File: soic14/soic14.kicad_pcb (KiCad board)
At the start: 2 copper layers, 15.2 x 17.8 mm, 2 parts, among them J1 bb2x7, U1 u2x7

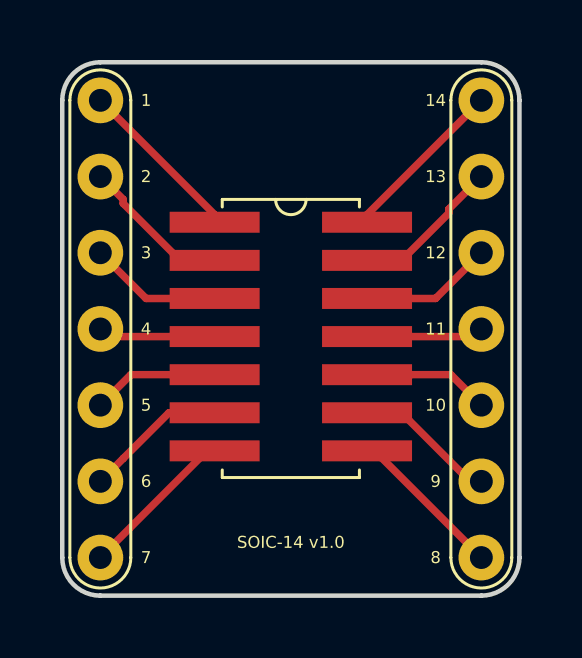
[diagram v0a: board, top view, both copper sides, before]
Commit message: Updated SOIC_SOP-SO footprints, added MSOP-TSSOP footprints
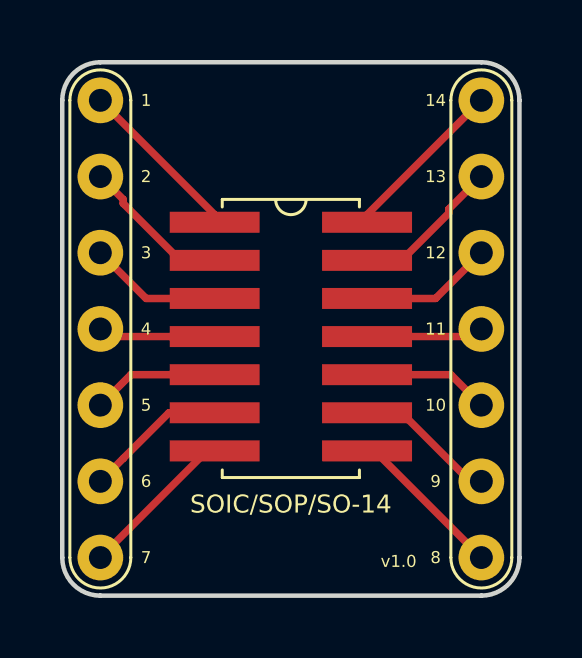
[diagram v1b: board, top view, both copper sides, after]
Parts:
- U1: value u2x7 -> SOIC/SOP/SO-14; footprint DevPc:soic-14 -> DevPcb:soic_sop_so-14
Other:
- board text added: "v1.0"
- board text removed: "SOIC-14 v1.0"
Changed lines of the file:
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@@
     (pad_to_mask_clearance 0.2)
     (aux_axis_origin 0 0)
-    (visible_elements FFFFFF7F)
+    (visible_elements 7FFFFFFF)
     (pcbplotparams
       (layerselection 0x010fc_ffffffff)
@@
     (add_net "Net-(J1-Pad9)")
   )
+  (module DevPcb:soic_sop_so-14 (layer F.Cu)
+    (at 138.176 94.107)
+    (tags "soic soic14 soic-14 soic-14-n sop so jedec")
+    (attr smd)
+    (fp_text reference U1 (at 0 11.684) (layer F.SilkS) hide
+      (effects (font (size 0.4 0.4) (thickness 0.1)))
+    )
+    (fp_text value SOIC/SOP/SO-14 (at 0 10.668) (layer F.SilkS)
+      (effects (font (size 0.6 0.6) (thickness 0.15)))
+    )
+    (fp_arc (start 0 0.508) (end -0.508 0.508) (angle -180) (layer F.SilkS) (width 0.1))
+    (fp_line (start 2.286 9.525) (end 2.286 9.779) (layer F.SilkS) (width 0.1))
+    (fp_line (start 2.286 9.779) (end -2.286 9.779) (layer F.SilkS) (width 0.1))
+    (fp_line (start -2.286 9.525) (end -2.286 9.779) (layer F.SilkS) (width 0.1))
+    (fp_line (start 2.286 0.508) (end 2.286 0.762) (layer F.SilkS) (width 0.1))
+    (fp_line (start -2.286 0.508) (end -2.286 0.762) (layer F.SilkS) (width 0.1))
+    (fp_line (start -2.286 0.508) (end 2.286 0.508) (layer F.SilkS) (width 0.1))
+    (pad 9 smd rect (at 2.54 7.62 90) (size 0.7 3) (layers F.Cu F.Paste F.Mask)
+      (net 9 "Net-(J1-Pad9)") (solder_mask_margin 0.1))
+    (pad 10 smd rect (at 2.54 6.35 90) (size 0.7 3) (layers F.Cu F.Paste F.Mask)
+      (net 10 "Net-(J1-Pad10)") (solder_mask_margin 0.1))
+    (pad 12 smd rect (at 2.54 3.81 90) (size 0.7 3) (layers F.Cu F.Paste F.Mask)
+      (net 12 "Net-(J1-Pad12)") (solder_mask_margin 0.1))
+    (pad 11 smd rect (at 2.54 5.08 90) (size 0.7 3) (layers F.Cu F.Paste F.Mask)
+      (net 11 "Net-(J1-Pad11)") (solder_mask_margin 0.1))
+    (pad 8 smd rect (at 2.54 8.89 90) (size 0.7 3) (layers F.Cu F.Paste F.Mask)
+      (net 8 "Net-(J1-Pad8)") (solder_mask_margin 0.1))
+    (pad 7 smd rect (at -2.54 8.89 90) (size 0.7 3) (layers F.Cu F.Paste F.Mask)
+      (net 7 "Net-(J1-Pad7)") (solder_mask_margin 0.1))
+    (pad 6 smd rect (at -2.54 7.62 90) (size 0.7 3) (layers F.Cu F.Paste F.Mask)
+      (net 6 "Net-(J1-Pad6)") (solder_mask_margin 0.1))
+    (pad 5 smd rect (at -2.54 6.35 90) (size 0.7 3) (layers F.Cu F.Paste F.Mask)
+      (net 5 "Net-(J1-Pad5)") (solder_mask_margin 0.1))
+    (pad 13 smd rect (at 2.54 2.54 90) (size 0.7 3) (layers F.Cu F.Paste F.Mask)
+      (net 13 "Net-(J1-Pad13)") (solder_mask_margin 0.1))
+    (pad 14 smd rect (at 2.54 1.27 90) (size 0.7 3) (layers F.Cu F.Paste F.Mask)
+      (net 14 "Net-(J1-Pad14)") (solder_mask_margin 0.1))
+    (pad 4 smd rect (at -2.54 5.08 90) (size 0.7 3) (layers F.Cu F.Paste F.Mask)
+      (net 4 "Net-(J1-Pad4)") (solder_mask_margin 0.1))
+    (pad 3 smd rect (at -2.54 3.81 90) (size 0.7 3) (layers F.Cu F.Paste F.Mask)
+      (net 3 "Net-(J1-Pad3)") (solder_mask_margin 0.1))
+    (pad 2 smd rect (at -2.54 2.54 90) (size 0.7 3) (layers F.Cu F.Paste F.Mask)
+      (net 2 "Net-(J1-Pad2)") (solder_mask_margin 0.1))
+    (pad 1 smd rect (at -2.54 1.27 90) (size 0.7 3) (layers F.Cu F.Paste F.Mask)
+      (net 1 "Net-(J1-Pad1)") (solder_mask_margin 0.1))
+    (model ${KISYS3DMOD}/Package_SO.3dshapes/SOIC-14_3.9x8.7mm_P1.27mm.step
+      (offset (xyz 0 -5.1 0))
+      (scale (xyz 1 1 1))
+      (rotate (xyz 0 0 0))
+    )
+  )
   (module DevPc:bb_2x7 (layer F.Cu)
     (at 131.826 91.313)
@@
       (net 14 "Net-(J1-Pad14)"))
   )
-  (module DevPc:soic-14 (layer F.Cu)
-    (at 138.176 94.107)
-    (tags "soic soic14 soic-14 soic-14-n jedec")
-    (attr smd)
-    (fp_text reference U1 (at 0.254 10.287) (layer F.SilkS) hide
-      (effects (font (size 0.4 0.4) (thickness 0.1)))
-    )
-    (fp_text value u2x7 (at 0 -0.5) (layer F.Fab) hide
-      (effects (font (size 1 1) (thickness 0.15)))
-    )
-    (fp_line (start -2.286 0.508) (end 2.286 0.508) (layer F.SilkS) (width 0.1))
-    (fp_line (start -2.286 0.508) (end -2.286 0.762) (layer F.SilkS) (width 0.1))
-    (fp_line (start 2.286 0.508) (end 2.286 0.762) (layer F.SilkS) (width 0.1))
-    (fp_line (start -2.286 9.525) (end -2.286 9.779) (layer F.SilkS) (width 0.1))
-    (fp_line (start 2.286 9.779) (end -2.286 9.779) (layer F.SilkS) (width 0.1))
-    (fp_line (start 2.286 9.525) (end 2.286 9.779) (layer F.SilkS) (width 0.1))
-    (fp_arc (start 0 0.508) (end -0.508 0.508) (angle -180) (layer F.SilkS) (width 0.1))
-    (pad 1 smd rect (at -2.54 1.27 90) (size 0.7 3) (layers F.Cu F.Paste F.Mask)
-      (net 1 "Net-(J1-Pad1)") (solder_mask_margin 0.1))
-    (pad 2 smd rect (at -2.54 2.54 90) (size 0.7 3) (layers F.Cu F.Paste F.Mask)
-      (net 2 "Net-(J1-Pad2)") (solder_mask_margin 0.1))
-    (pad 3 smd rect (at -2.54 3.81 90) (size 0.7 3) (layers F.Cu F.Paste F.Mask)
-      (net 3 "Net-(J1-Pad3)") (solder_mask_margin 0.1))
-    (pad 4 smd rect (at -2.54 5.08 90) (size 0.7 3) (layers F.Cu F.Paste F.Mask)
-      (net 4 "Net-(J1-Pad4)") (solder_mask_margin 0.1))
-    (pad 14 smd rect (at 2.54 1.27 90) (size 0.7 3) (layers F.Cu F.Paste F.Mask)
-      (net 14 "Net-(J1-Pad14)") (solder_mask_margin 0.1))
-    (pad 13 smd rect (at 2.54 2.54 90) (size 0.7 3) (layers F.Cu F.Paste F.Mask)
-      (net 13 "Net-(J1-Pad13)") (solder_mask_margin 0.1))
-    (pad 5 smd rect (at -2.54 6.35 90) (size 0.7 3) (layers F.Cu F.Paste F.Mask)
-      (net 5 "Net-(J1-Pad5)") (solder_mask_margin 0.1))
-    (pad 6 smd rect (at -2.54 7.62 90) (size 0.7 3) (layers F.Cu F.Paste F.Mask)
-      (net 6 "Net-(J1-Pad6)") (solder_mask_margin 0.1))
-    (pad 7 smd rect (at -2.54 8.89 90) (size 0.7 3) (layers F.Cu F.Paste F.Mask)
-      (net 7 "Net-(J1-Pad7)") (solder_mask_margin 0.1))
-    (pad 8 smd rect (at 2.54 8.89 90) (size 0.7 3) (layers F.Cu F.Paste F.Mask)
-      (net 8 "Net-(J1-Pad8)") (solder_mask_margin 0.1))
-    (pad 11 smd rect (at 2.54 5.08 90) (size 0.7 3) (layers F.Cu F.Paste F.Mask)
-      (net 11 "Net-(J1-Pad11)") (solder_mask_margin 0.1))
-    (pad 12 smd rect (at 2.54 3.81 90) (size 0.7 3) (layers F.Cu F.Paste F.Mask)
-      (net 12 "Net-(J1-Pad12)") (solder_mask_margin 0.1))
-    (pad 10 smd rect (at 2.54 6.35 90) (size 0.7 3) (layers F.Cu F.Paste F.Mask)
-      (net 10 "Net-(J1-Pad10)") (solder_mask_margin 0.1))
-    (pad 9 smd rect (at 2.54 7.62 90) (size 0.7 3) (layers F.Cu F.Paste F.Mask)
-      (net 9 "Net-(J1-Pad9)") (solder_mask_margin 0.1))
-    (model ${KISYS3DMOD}/Package_SO.3dshapes/SOIC-14_3.9x8.7mm_P1.27mm.step
-      (offset (xyz 0 -5.1 0))
-      (scale (xyz 1 1 1))
-      (rotate (xyz 0 0 0))
-    )
-  )
-  (gr_text "SOIC-14 v1.0" (at 138.176 106.045) (layer F.SilkS)
-    (effects (font (size 0.4 0.4) (thickness 0.1)))
+  (gr_text v1.0 (at 142.367 106.68) (layer F.SilkS)
+    (effects (font (size 0.4 0.4) (thickness 0.1)) (justify right))
   )
   (gr_line (start 145.796 106.553) (end 145.796 91.313) (layer Edge.Cuts) (width 0.15))
